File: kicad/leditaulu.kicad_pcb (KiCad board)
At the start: 2 copper layers, 45 parts, among them CON1 12V input, P1 Programming header, P2 I2C addr select, P4 I2C addr select, P5 Interconnect 1, P6 Interconnect 2, U1 ESP-12E, U2 TLC59116IPWR, U3 LD1086, U4 nRF24L01+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

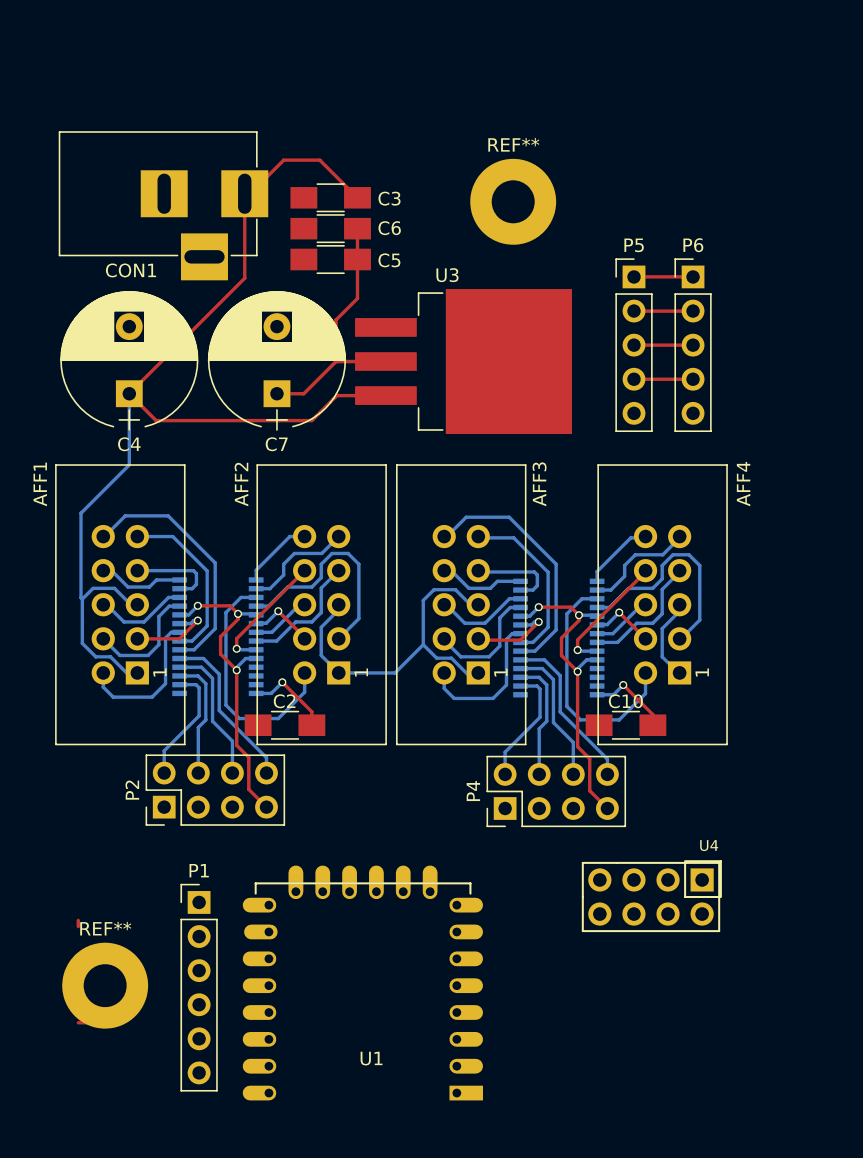
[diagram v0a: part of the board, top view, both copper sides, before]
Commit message: Add buttons, continue routing
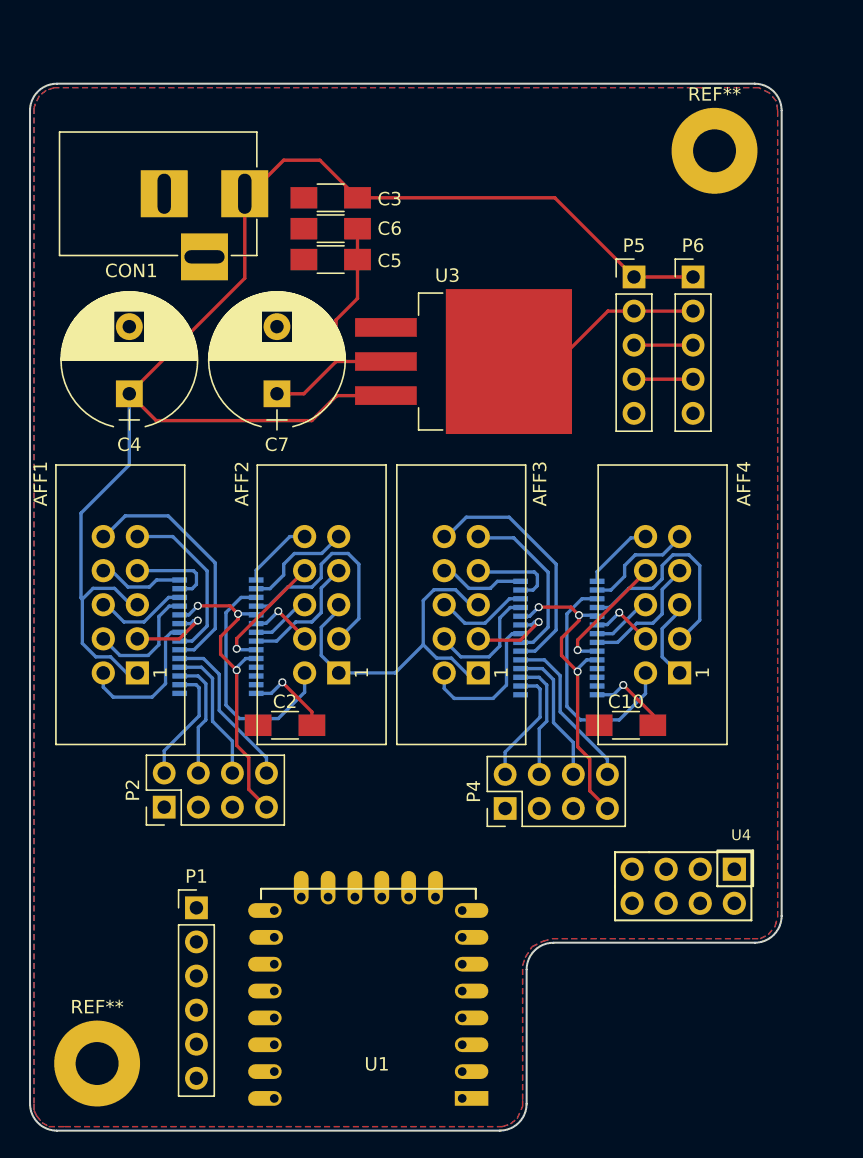
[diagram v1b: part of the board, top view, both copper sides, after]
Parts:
- moved REF** 15.5 mm to (94.0, 107.0)
- moved REF** 5.83 mm to (48.0, 175.0)
- moved U4 2.53 mm to (97.0, 159.0)
- moved U1 0.57 mm to (75.2, 177.6)
- moved P1 0.45 mm to (55.4, 163.4)
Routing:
- net VCC: track 117.0 -> 140.0 mm
- net 3V3: track 42.2 -> 53.1 mm
- net (no net): track 1.44 -> 0.00 mm
- added copper zone on B.Cu, net Earth
- added copper zone on F.Cu, net Earth
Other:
- board outline added: 56 x 78 mm
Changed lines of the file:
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@@
   (general
     (links 152)
-    (no_connects 88)
-    (area 37.257143 96.65 238.250002 188.875001)
+    (no_connects 86)
+    (area 42.924999 101.924999 99.075001 180.075001)
     (thickness 1.6)
-    (drawings 0)
-    (tracks 330)
+    (drawings 12)
+    (tracks 332)
     (zones 0)
     (modules 45)
@@
     (mod_text_size 1 1)
     (mod_text_width 0.15)
-    (pad_size 1.524 1.524)
-    (pad_drill 0.762)
+    (pad_size 2.5 1.1)
+    (pad_drill 0)
     (pad_to_mask_clearance 0.2)
     (aux_axis_origin 0 0)
@@
   )
   (module Mounting_Holes:MountingHole_3.2mm_M3_Pad (layer F.Cu)
-    (at 48.6 169.2)
+    (at 48 175)
     (descr "Mounting Hole 3.2mm, M3")
     (tags "mounting hole 3.2mm m3")
@@
   )
   (module ESP8266:ESP-12E (layer F.Cu)
-    (at 74.8 177.2 180)
+    (at 75.2 177.6 180)
     (descr "Module, ESP-8266, ESP-12, 16 pad, SMD")
     (tags "Module ESP-8266 ESP8266")
@@
   )
   (module mysensors_radios:NRF24L01 (layer F.Cu)
-    (at 94.6 159.8)
+    (at 97 159)
     (descr NRF24L01)
     (tags "nRF 24 NRF24L01 NRF24L01+")
@@
   )
   (module Pin_Headers:Pin_Header_Straight_1x06_Pitch2.54mm (layer F.Cu)
-    (at 55.6 163)
+    (at 55.4 163.4)
     (descr "Through hole straight pin header, 1x06, 2.54mm pitch, single row")
     (tags "Through hole pin header THT 1x06 2.54mm single row")
@@
   )
   (module Mounting_Holes:MountingHole_3.2mm_M3_Pad (layer F.Cu)
-    (at 79 110.8)
+    (at 94 107)
     (descr "Mounting Hole 3.2mm, M3")
     (tags "mounting hole 3.2mm m3")
@@
     (pad 1 thru_hole circle (at 0 0) (size 6.4 6.4) (drill 3.2) (layers *.Cu *.Mask))
   )
-  (segment (start 46.6 164.34) (end 46.6 164.8) (width 0.25) (layer F.Cu) (net 0))
-  (segment (start 46.6 169.42) (end 46.92 169.42) (width 0.25) (layer F.Cu) (net 0))
-  (segment (start 46.6 171.96) (end 47.26 171.96) (width 0.25) (layer F.Cu) (net 0))
+  (gr_arc (start 45 178) (end 45 180) (angle 90) (layer Edge.Cuts) (width 0.15))
+  (gr_arc (start 78 178) (end 80 178) (angle 90) (layer Edge.Cuts) (width 0.15))
+  (gr_arc (start 82 168) (end 80 168) (angle 90) (layer Edge.Cuts) (width 0.15))
+  (gr_arc (start 97 164) (end 99 164) (angle 90) (layer Edge.Cuts) (width 0.15))
+  (gr_arc (start 97 104) (end 97 102) (angle 90) (layer Edge.Cuts) (width 0.15))
+  (gr_arc (start 45 104) (end 43 104) (angle 90) (layer Edge.Cuts) (width 0.15))
+  (gr_line (start 43 178) (end 43 104) (angle 90) (layer Edge.Cuts) (width 0.15))
+  (gr_line (start 78 180) (end 45 180) (angle 90) (layer Edge.Cuts) (width 0.15))
+  (gr_line (start 80 168) (end 80 178) (angle 90) (layer Edge.Cuts) (width 0.15))
+  (gr_line (start 97 166) (end 82 166) (angle 90) (layer Edge.Cuts) (width 0.15))
+  (gr_line (start 99 104) (end 99 164) (angle 90) (layer Edge.Cuts) (width 0.15))
+  (gr_line (start 45 102) (end 97 102) (angle 90) (layer Edge.Cuts) (width 0.15))
+  (segment (start 67.4 110.5) (end 82.1 110.5) (width 0.25) (layer F.Cu) (net 1) (status 400000))
+  (segment (start 82.1 110.5) (end 88 116.4) (width 0.25) (layer F.Cu) (net 1) (status 800000))
   (segment (start 66 145.9) (end 70.2 145.9) (width 0.25) (layer B.Cu) (net 1))
   (segment (start 70.2 145.9) (end 72.3 143.8) (width 0.25) (layer B.Cu) (net 1))
@@
   (segment (start 87.76 135.84) (end 88.86 135.84) (width 0.25) (layer B.Cu) (net 33))
   (segment (start 85.25 139.075) (end 85.25 138.35) (width 0.25) (layer B.Cu) (net 33))
+  (segment (start 78.68 122.7) (end 82.3 122.7) (width 0.25) (layer F.Cu) (net 34) (status C00000))
+  (segment (start 82.3 122.7) (end 86.06 118.94) (width 0.25) (layer F.Cu) (net 34) (status 400000))
+  (segment (start 86.06 118.94) (end 88 118.94) (width 0.25) (layer F.Cu) (net 34) (status 800000))
   (segment (start 89.4 150) (end 89.4 149) (width 0.25) (layer F.Cu) (net 34))
   (segment (start 86.475 147.525) (end 85.25 147.525) (width 0.25) (layer B.Cu) (net 34))
@@
   (segment (start 88 121.48) (end 92.4 121.48) (width 0.25) (layer F.Cu) (net 48))
   (segment (start 88 124.02) (end 92.4 124.02) (width 0.25) (layer F.Cu) (net 49))
+  (zone (net 35) (net_name Earth) (layer F.Cu) (hatch edge 0.508)
+    (connect_pads (clearance 0.508))
+    (min_thickness 0.254)
+    (fill (arc_segments 16) (thermal_gap 0.508) (thermal_bridge_width 0.508))
+    (polygon
+      (pts
+        (xy 93.1 102.3) (xy 44.8 102.3) (xy 44.2 102.5) (xy 43.7 102.9) (xy 43.4 103.5)
+        (xy 43.3 103.8) (xy 43.3 106) (xy 43.3 178) (xy 43.3 178.5) (xy 43.5 178.9)
+        (xy 43.9 179.4) (xy 44.4 179.7) (xy 45.6 179.7) (xy 78.2 179.7) (xy 78.8 179.5)
+        (xy 79.3 179.1) (xy 79.7 178.2) (xy 79.7 177.7) (xy 79.7 167.7) (xy 79.9 167.1)
+        (xy 80.4 166.3) (xy 81.2 165.9) (xy 81.9 165.7) (xy 96.8 165.7) (xy 97.4 165.7)
+        (xy 98 165.4) (xy 98.5 164.8) (xy 98.7 164.1) (xy 98.7 158.1) (xy 98.7 104)
+        (xy 98.6 103.3) (xy 98.1 102.7) (xy 97.3 102.3) (xy 93 102.3)
+      )
+    )
+  )
+  (zone (net 35) (net_name Earth) (layer B.Cu) (hatch edge 0.508)
+    (connect_pads (clearance 0.508))
+    (min_thickness 0.254)
+    (fill (arc_segments 16) (thermal_gap 0.508) (thermal_bridge_width 0.508))
+    (polygon
+      (pts
+        (xy 93.1 102.3) (xy 44.8 102.3) (xy 44.2 102.5) (xy 43.7 102.9) (xy 43.4 103.5)
+        (xy 43.3 103.8) (xy 43.3 106) (xy 43.3 178) (xy 43.3 178.5) (xy 43.5 178.9)
+        (xy 43.9 179.4) (xy 44.4 179.7) (xy 45.6 179.7) (xy 78.2 179.7) (xy 78.8 179.5)
+        (xy 79.3 179.1) (xy 79.7 178.2) (xy 79.7 177.7) (xy 79.7 167.7) (xy 79.9 167.1)
+        (xy 80.4 166.3) (xy 81.2 165.9) (xy 81.9 165.7) (xy 96.8 165.7) (xy 97.4 165.7)
+        (xy 98 165.4) (xy 98.5 164.8) (xy 98.7 164.1) (xy 98.7 158.1) (xy 98.7 104)
+        (xy 98.6 103.3) (xy 98.1 102.7) (xy 97.3 102.3) (xy 93 102.3)
+      )
+    )
+  )
 )

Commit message: Finish routing
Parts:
- added R19: 10K, Resistors_SMD:R_1206_HandSoldering, B.Cu at (66.9, 175.7)
- added SW1: SW_RESET, Buttons_Switches_SMD:SW_SPST_B3S-1000, F.Cu at (49.0, 165.1)
- added SW2: SW_FLASH, Buttons_Switches_SMD:SW_SPST_B3S-1000, F.Cu at (49.0, 174.9)
- C1, C8, C9, R1, R10, R12, R17, R2, R3, R4, R5: moved to B.Cu
- U1: footprint ESP8266:ESP-12E -> ESP8266:ESP-12E_SMD
- moved R10 190.1 mm to (48.8, 150.5), turned to 180 degrees
- moved R5 179.3 mm to (66.9, 168.2)
- moved R4 169.6 mm to (66.9, 170.7)
- moved R9 167.2 mm to (48.8, 159.7), turned to 180 degrees
- moved R16 165.0 mm to (74.2, 159.6), turned to 180 degrees
- moved R3 161.9 mm to (66.9, 173.2)
- moved R8 159.1 mm to (48.8, 157.4), turned to 180 degrees
- moved C9 150.9 mm to (94.5, 155.0), turned to 90 degrees
- moved R15 149.7 mm to (74.2, 157.3), turned to 180 degrees
- moved R7 149.6 mm to (48.8, 155.1), turned to 180 degrees
- moved R17 147.5 mm to (74.2, 150.4), turned to 180 degrees
- moved R2 146.5 mm to (61.4, 173.7), turned to 90 degrees
- moved R6 142.3 mm to (48.8, 152.8), turned to 180 degrees
- moved R14 140.5 mm to (74.2, 155.0), turned to 180 degrees
- moved R18 138.0 mm to (92.2, 152.8)
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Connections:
- P1 pad 2: ESP_GPIO0 -> Earth
- P1 pad 3: ESP_RST -> (no net)
- P1 pad 6: Earth -> (no net)
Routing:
- net 3V3: track 53.1 -> 252.7 mm, vias 2 -> 6
- net SDA: track 4.40 -> 120.3 mm, vias 0 -> 6
- net SCL: track 4.40 -> 117.6 mm, vias 0 -> 3
- net Earth: track 49.1 -> 132.2 mm, vias 6 -> 12
- net ESP_RST: track 0.00 -> 43.5 mm, vias 0 -> 2
- net VCC: track 140.0 -> 182.9 mm, vias 0 -> 1
- net NRF_CE: track 0.00 -> 39.2 mm, vias 0 -> 1
- net NRF_CSN: track 0.00 -> 37.7 mm, vias 0 -> 1
- net ESP_GPIO0: track 0.00 -> 29.3 mm, vias 0 -> 3
- net SPI_CLK: track 0.00 -> 23.1 mm, vias 0 -> 1
- net Net-(P2-Pad8): track 12.3 -> 29.7 mm
- net Net-(P4-Pad8): track 12.3 -> 29.6 mm
- net MOSI: track 0.00 -> 16.6 mm, vias 0 -> 1
- net MISO: track 0.00 -> 15.9 mm
- net Net-(P2-Pad6): track 10.5 -> 21.7 mm
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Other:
- board text added: "3V3"
- board text added: "FLASH"
- board text added: "GND"
- board text added: "RESET"
- board text added: "RX"
- board text added: "SCL"
- board text added: "SDA"
- board text added: "TX"
- board text added: "VCC"
- board text added: "Wireless LED display driver v1.0 2017 jaakkos@gmail.com sakari.tanskanen@gmail.com"

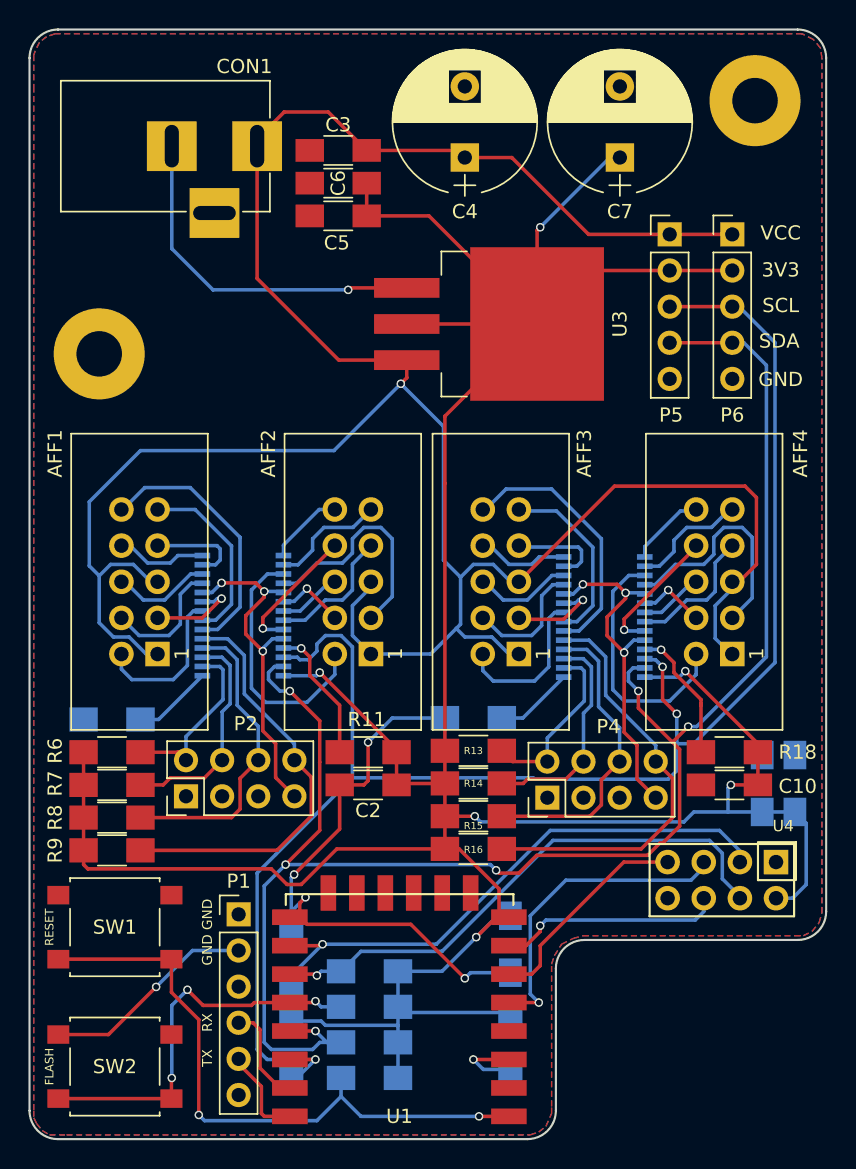
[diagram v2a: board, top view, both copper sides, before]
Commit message: Add power supply protection; misc. fixes
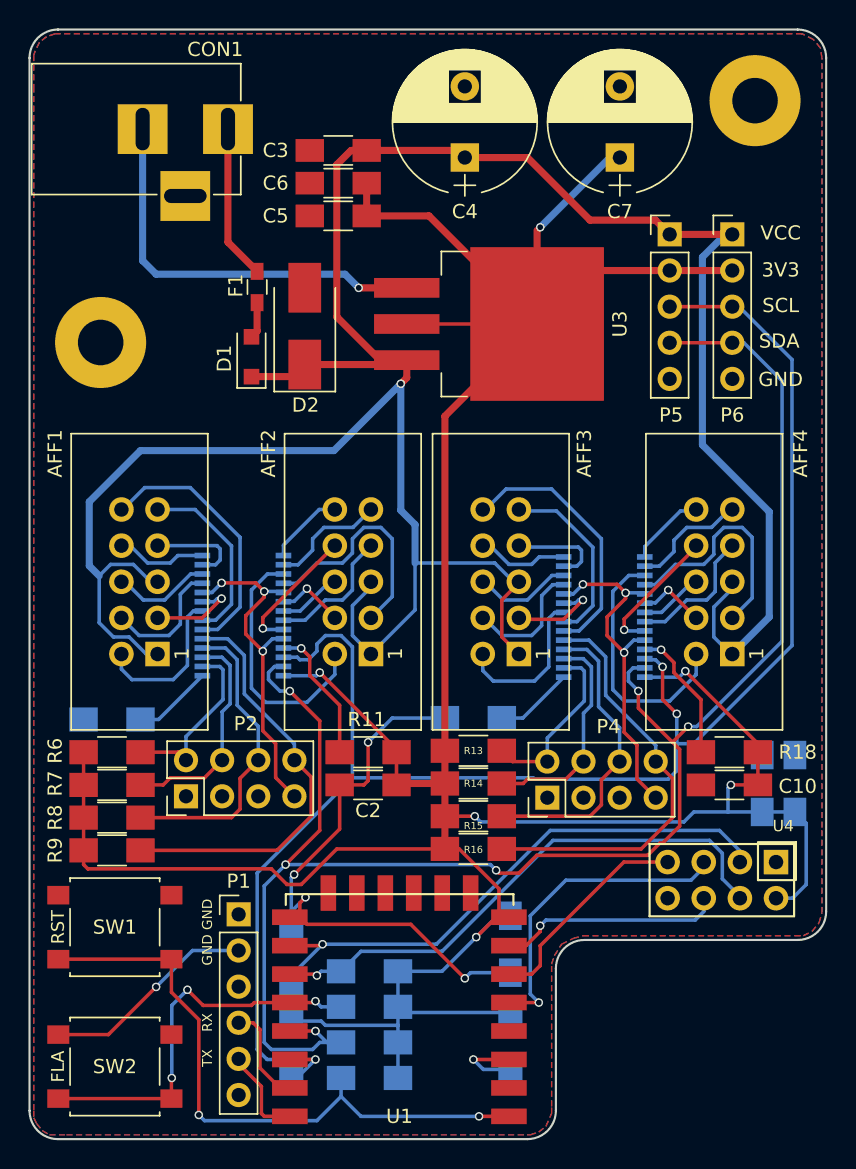
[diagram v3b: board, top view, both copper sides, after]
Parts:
- added D1: Schottky, Diodes_SMD:D_SOD-123F, F.Cu at (58.6, 125.0)
- added D2: Zener 30V, Diodes_SMD:D_SMB_Handsoldering, F.Cu at (62.4, 122.8)
- added F1: 2.5A, Resistors_SMD:R_0603_HandSoldering, F.Cu at (59.0, 120.1)
- moved CON1 2.38 mm to (57.0, 109.0)
- moved REF** 0.81 mm to (48.0, 124.0)
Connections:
- AFF1 pad 1: VCC -> VCC_PROT
- AFF1 pad 5: VCC -> VCC_PROT
- AFF2 pad 1: VCC -> VCC_PROT
- AFF2 pad 5: VCC -> VCC_PROT
- AFF3 pad 1: VCC -> VCC_PROT
- AFF3 pad 5: VCC -> VCC_PROT
- AFF4 pad 1: VCC -> VCC_PROT
- AFF4 pad 5: VCC -> VCC_PROT
- C3 pad 1: VCC -> VCC_PROT
- C4 pad 1: VCC -> VCC_PROT
- P5 pad 1: VCC -> VCC_PROT
- P6 pad 1: VCC -> VCC_PROT
- U3 pad 3: VCC -> VCC_PROT
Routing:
- net VCC_PROT: track 0.00 -> 186.2 mm, vias 0 -> 1
- net VCC: track 182.9 -> 10.8 mm, vias 1 -> 0
- net Earth: track 132.2 -> 135.8 mm
- net Net-(D1-Pad2): track 0.00 -> 2.57 mm
- net SCL: track 117.6 -> 118.5 mm
- net SDA: track 120.3 -> 121.2 mm
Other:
- board text added: "FLA"
- board text added: "RST"
- board text removed: "FLASH"
- board text removed: "RESET"

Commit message: Version 1.0
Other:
- board text added: "12-24VDC Polarity: +"
- board text added: "Fuse 0603 2.5A 32V"
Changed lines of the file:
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@@
     (links 164)
     (no_connects 0)
-    (area 42.924999 101.924999 99.075001 180.075001)
+    (area 36.657143 101.825 105.342858 188.075001)
     (thickness 1.6)
-    (drawings 24)
+    (drawings 26)
     (tracks 661)
     (zones 0)
@@
   )
   (setup
-    (last_trace_width 0.5)
+    (last_trace_width 0.25)
     (user_trace_width 0.5)
     (trace_clearance 0.2)
@@
     (fp_circle (center 0 0) (end 3.45 0) (layer F.CrtYd) (width 0.05))
     (pad 1 thru_hole circle (at 0 0) (size 6.4 6.4) (drill 3.2) (layers *.Cu *.Mask))
+  )
+  (gr_text "12-24VDC\nPolarity: +" (at 48 115.5) (layer F.SilkS)
+    (effects (font (size 1 1) (thickness 0.2)))
+  )
+  (gr_text "Fuse 0603\n2.5A 32V" (at 55.7 120 90) (layer F.SilkS)
+    (effects (font (size 0.6 0.6) (thickness 0.1)))
   )
   (gr_text RST (at 45 165.1 90) (layer F.SilkS)
@@
   (segment (start 89 157.7) (end 74.7 157.7) (width 0.25) (layer B.Cu) (net 34))
   (segment (start 89.7 157) (end 89 157.7) (width 0.25) (layer B.Cu) (net 34))
-  (segment (start 69.52 122.7) (end 78.68 122.7) (width 0.25) (layer F.Cu) (net 34) (status 30))
+  (segment (start 69.52 122.7) (end 78.68 122.7) (width 0.5) (layer F.Cu) (net 34) (status 30))
   (segment (start 78.68 122.7) (end 78.68 127.42) (width 0.25) (layer F.Cu) (net 34) (status 30))
   (segment (start 94.5 157) (end 96.8 157) (width 0.25) (layer B.Cu) (net 34) (status 30))
